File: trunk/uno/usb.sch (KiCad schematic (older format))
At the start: 20 parts, among them U3 ATMEGA16U2-MU(R), X2 USB-MINI-AB

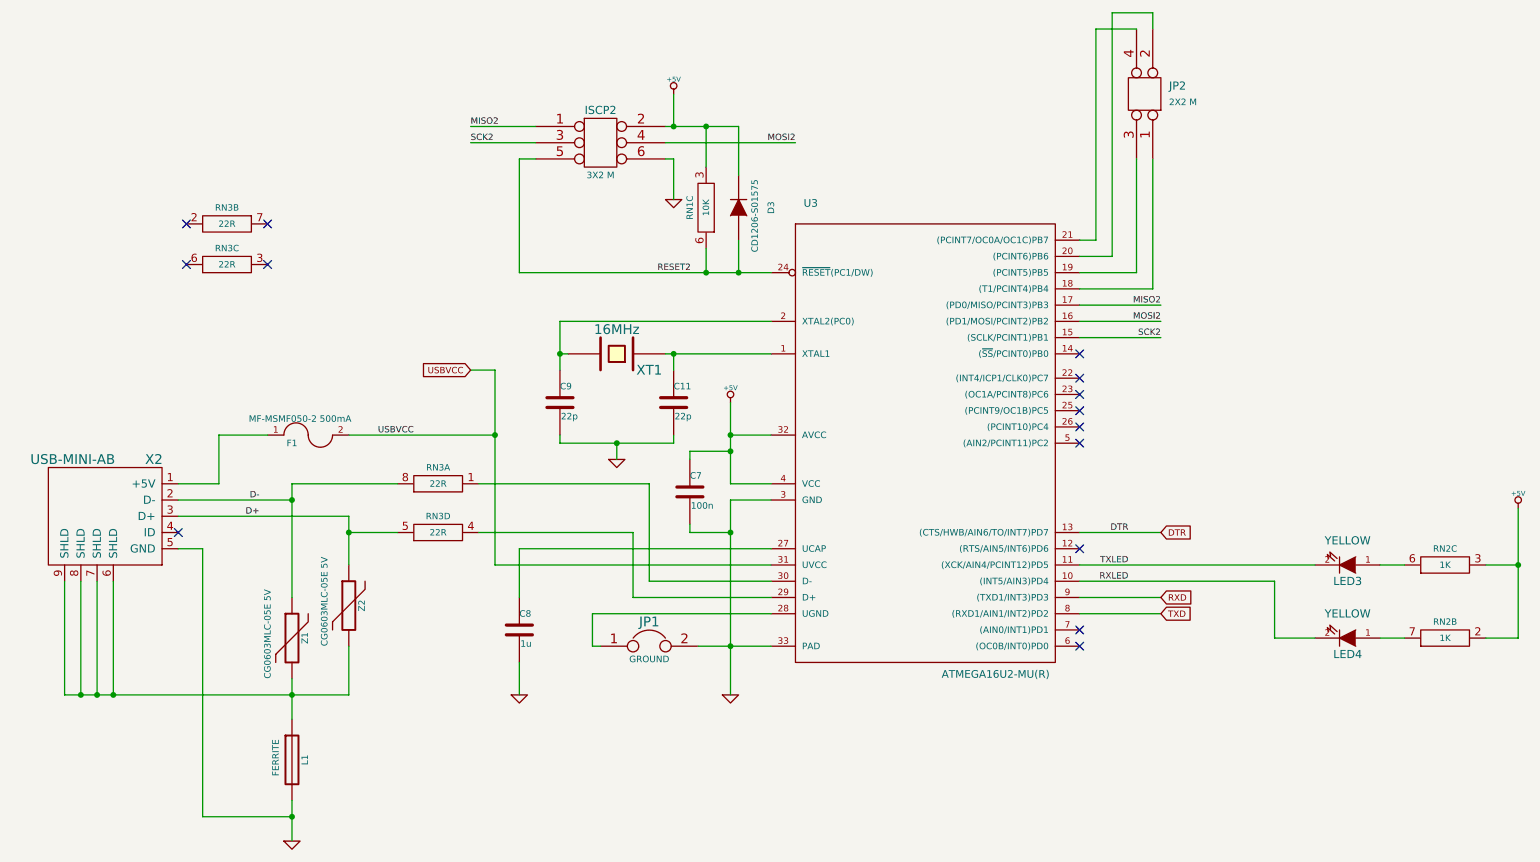
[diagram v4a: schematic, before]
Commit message: All components placed. Some routing started.
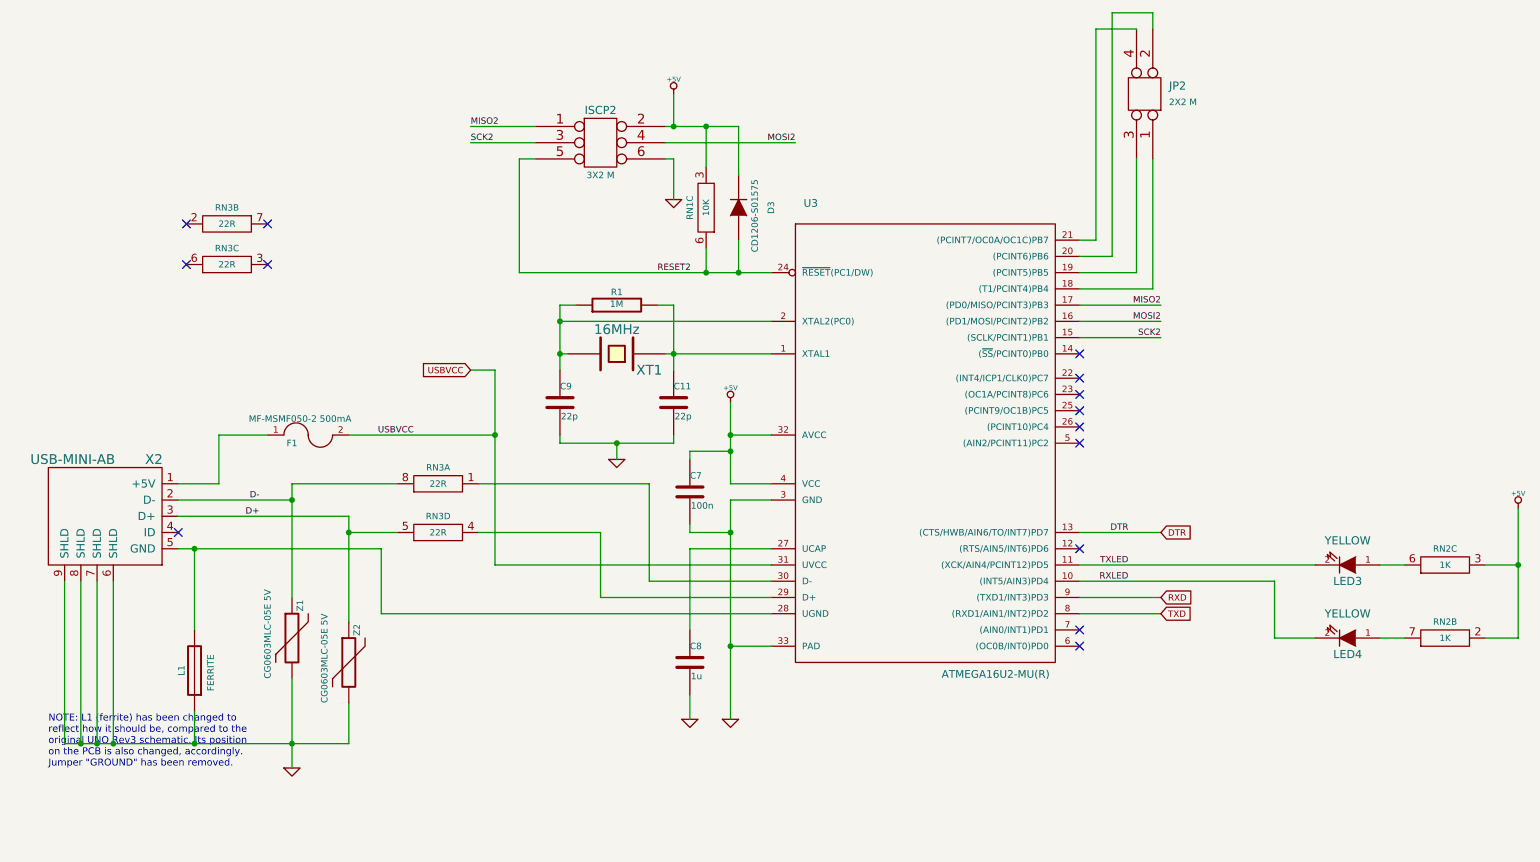
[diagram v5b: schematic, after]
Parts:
- removed JP1: GROUND, JSOLD, symbol JUMPER
- added R1: 1M, ~, symbol R
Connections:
- net GND: now also L1.1, X2.6 (SHLD), X2.7 (SHLD), X2.8 (SHLD), X2.9 (SHLD), Z1.2, Z2.2; no longer L1.2, X2.5 (GND)
- net at C11.1, U3.1 (XTAL1), XT1.1: now also R1.2
- net at C9.1, U3.2 (XTAL2(PC0)), XT1.2: now also R1.1
- net at U3.28 (UGND): now also L1.2, X2.5 (GND)
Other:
- note added: "NOTE: L1 (ferrite) has been changed to\nreflect how it should be, compared to the\noriginal UNO Rev3 schematic. Its position\non the PCB is also changed, accordingly.\nJumper "GROUND" has been removed."
- moved on the sheet: C8, L1, Z2
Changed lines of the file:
@@
 Sheet 2 3
 Title "KiCADuino UNO Rev3"
-Date "25 jul 2013"
+Date "26 jul 2013"
 Rev "0.1"
 Comp "Gruvin & Co"
@@
 L GND #PWR014
 U 1 1 51EFEC35
-P 5450 5500
-F 0 "#PWR014" H 5450 5500 30  0001 C CNN
-F 1 "GND" H 5450 5430 30  0001 C CNN
-F 2 "" H 5450 5500 60  0000 C CNN
-F 3 "" H 5450 5500 60  0000 C CNN
-	1    5450 5500
-	1    0    0    -1
-$EndComp
-$Comp
-L JUMPER JP1
-U 1 1 51EFED7A
-P 4950 5200
-F 0 "JP1" H 4950 5350 60  0000 C CNN
-F 1 "GROUND" H 4950 5120 40  0000 C CNN
-F 2 "JSOLD" H 4950 5200 60  0001 C CNN
-F 3 "~" H 4950 5200 60  0000 C CNN
-	1    4950 5200
+P 5450 5650
+F 0 "#PWR014" H 5450 5650 30  0001 C CNN
+F 1 "GND" H 5450 5580 30  0001 C CNN
+F 2 "" H 5450 5650 60  0000 C CNN
+F 3 "" H 5450 5650 60  0000 C CNN
+	1    5450 5650
 	1    0    0    -1
 $EndComp
@@
 U 1 1 51F00052
 P 2750 5150
-F 0 "Z1" V 2830 5150 40  0000 C CNN
+F 0 "Z1" V 2800 5350 40  0000 C CNN
 F 1 "CG0603MLC-05E 5V" V 2600 4900 40  0000 L CNN
 F 2 "" V 2680 5150 30  0001 C CNN
@@
 L VARISTOR Z2
 U 1 1 51F00069
-P 3100 4950
-F 0 "Z2" V 3180 4950 40  0000 C CNN
-F 1 "CG0603MLC-05E 5V" V 2950 4700 40  0000 L CNN
-F 2 "" V 3030 4950 30  0001 C CNN
-F 3 "~" H 3100 4950 30  0000 C CNN
-	1    3100 4950
+P 3100 5300
+F 0 "Z2" V 3150 5500 40  0000 C CNN
+F 1 "CG0603MLC-05E 5V" V 2950 5050 40  0000 L CNN
+F 2 "" V 3030 5300 30  0001 C CNN
+F 3 "~" H 3100 5300 30  0000 C CNN
+	1    3100 5300
 	1    0    0    -1
 $EndComp
@@
 L GND #PWR017
 U 1 1 51F000AD
-P 2750 6400
-F 0 "#PWR017" H 2750 6400 30  0001 C CNN
-F 1 "GND" H 2750 6330 30  0001 C CNN
-F 2 "" H 2750 6400 60  0000 C CNN
-F 3 "" H 2750 6400 60  0000 C CNN
-	1    2750 6400
+P 2750 5950
+F 0 "#PWR017" H 2750 5950 30  0001 C CNN
+F 1 "GND" H 2750 5880 30  0001 C CNN
+F 2 "" H 2750 5950 60  0000 C CNN
+F 3 "" H 2750 5950 60  0000 C CNN
+	1    2750 5950
 	1    0    0    -1
 $EndComp
@@
 L FERRITE L1
 U 1 1 51F0018C
-P 2750 5900
-F 0 "L1" V 2830 5900 40  0000 C CNN
-F 1 "FERRITE" V 2650 5800 40  0000 L CNN
-F 2 "SM0805" V 2680 5900 30  0001 C CNN
-F 3 "~" H 2750 5900 30  0000 C CNN
-	1    2750 5900
-	1    0    0    -1
-$EndComp
-Wire Wire Line
-	5050 3400 5700 3400
+P 2150 5350
+F 0 "L1" V 2230 5350 40  0000 C CNN
+F 1 "FERRITE" V 2050 5250 40  0000 L CNN
+F 2 "SM0805" V 2080 5350 30  0001 C CNN
+F 3 "~" H 2150 5350 30  0000 C CNN
+	1    2150 5350
+	-1   0    0    1
+$EndComp
+Wire Wire Line
+	5050 3400 5100 3400
+Wire Wire Line
+	5100 3400 5700 3400
 Wire Wire Line
 	5700 3200 4400 3200
 Wire Wire Line
-	4400 3200 4400 3500
+	4400 3100 4400 3200
+Wire Wire Line
+	4400 3200 4400 3400
+Wire Wire Line
+	4400 3400 4400 3500
 Wire Wire Line
 	4400 3400 4450 3400
 Wire Wire Line
-	5100 3500 5100 3400
+	5100 3100 5100 3400
+Wire Wire Line
+	5100 3400 5100 3500
 Connection ~ 5100 3400
 Connection ~ 4400 3400
@@
 	4400 3900 4400 3950
 Wire Wire Line
-	4400 3950 5100 3950
+	4400 3950 4750 3950
+Wire Wire Line
+	4750 3950 5100 3950
 Wire Wire Line
 	5100 3950 5100 3900
@@
 	5450 4200 5700 4200
 Wire Wire Line
-	5450 3700 5450 4200
+	5450 3700 5450 3900
+Wire Wire Line
+	5450 3900 5450 4000
+Wire Wire Line
+	5450 4000 5450 4200
 Wire Wire Line
 	5700 3900 5450 3900
@@
 	5700 4300 5450 4300
 Wire Wire Line
-	5450 4300 5450 5500
-Wire Wire Line
-	5250 5200 5700 5200
+	5450 4300 5450 4500
+Wire Wire Line
+	5450 4500 5450 5200
+Wire Wire Line
+	5450 5200 5450 5650
 Connection ~ 5450 5200
 Wire Wire Line
-	5700 5000 4600 5000
-Wire Wire Line
-	4600 5000 4600 5200
-Wire Wire Line
-	4600 5200 4650 5200
-Wire Wire Line
 	7600 3100 8100 3100
 Wire Wire Line
@@
 	5100 1800 5100 2000
 Wire Wire Line
-	5050 2000 5500 2000
+	5050 2000 5100 2000
+Wire Wire Line
+	5100 2000 5300 2000
+Wire Wire Line
+	5300 2000 5500 2000
 Wire Wire Line
 	5050 2100 5850 2100
@@
 	4250 2000 3850 2000
 Wire Wire Line
-	4150 2900 5700 2900
+	4150 2900 5300 2900
+Wire Wire Line
+	5300 2900 5500 2900
+Wire Wire Line
+	5500 2900 5700 2900
 Wire Wire Line
 	4150 2900 4150 2200
@@
 	7600 5000 8100 5000
 Wire Wire Line
-	2750 6150 2750 6400
-Wire Wire Line
-	2750 5400 2750 5650
-Wire Wire Line
-	3100 5500 3100 5200
-Connection ~ 2750 5500
+	2750 5400 2750 5800
+Wire Wire Line
+	2750 5800 2750 5950
+Wire Wire Line
+	3100 5800 3100 5550
+Connection ~ 2750 5800
 Wire Wire Line
 	2050 4300 2750 4300
 Wire Wire Line
-	2750 4200 2750 4900
+	2750 4200 2750 4300
+Wire Wire Line
+	2750 4300 2750 4900
 Wire Wire Line
 	2750 4200 3400 4200
@@
 	2050 4400 3100 4400
 Wire Wire Line
-	3100 4400 3100 4700
+	3100 4400 3100 4500
+Wire Wire Line
+	3100 4500 3100 5050
 Wire Wire Line
 	3100 4500 3400 4500
@@
 Connection ~ 2750 4300
 Wire Wire Line
-	3900 4500 4850 4500
-Wire Wire Line
-	4850 4500 4850 4900
-Wire Wire Line
-	4850 4900 5700 4900
+	3900 4500 4650 4500
+Wire Wire Line
+	4650 4500 4650 4900
+Wire Wire Line
+	4650 4900 5700 4900
 Wire Wire Line
 	3900 4200 4950 4200
@@
 L C C8
 U 1 1 51F0053A
-P 4150 5100
-F 0 "C8" H 4150 5200 40  0000 L CNN
-F 1 "1u" H 4156 5015 40  0000 L CNN
-F 2 "SM0603_Capa" H 4188 4950 30  0001 C CNN
-F 3 "~" H 4150 5100 60  0000 C CNN
-	1    4150 5100
-	1    0    0    -1
-$EndComp
-Wire Wire Line
-	4150 5300 4150 5500
+P 5200 5300
+F 0 "C8" H 5200 5400 40  0000 L CNN
+F 1 "1u" H 5206 5215 40  0000 L CNN
+F 2 "SM0603_Capa" H 5238 5150 30  0001 C CNN
+F 3 "~" H 5200 5300 60  0000 C CNN
+	1    5200 5300
+	1    0    0    -1
+$EndComp
+Wire Wire Line
+	5200 5500 5200 5650
 $Comp
 L GND #PWR018
 U 1 1 51F005F8
-P 4150 5500
-F 0 "#PWR018" H 4150 5500 30  0001 C CNN
-F 1 "GND" H 4150 5430 30  0001 C CNN
-F 2 "" H 4150 5500 60  0000 C CNN
-F 3 "" H 4150 5500 60  0000 C CNN
-	1    4150 5500
+P 5200 5650
+F 0 "#PWR018" H 5200 5650 30  0001 C CNN
+F 1 "GND" H 5200 5580 30  0001 C CNN
+F 2 "" H 5200 5650 60  0000 C CNN
+F 3 "" H 5200 5650 60  0000 C CNN
+	1    5200 5650
 	1    0    0    -1
 $EndComp
@@
 	5200 4000 5450 4000
 Connection ~ 5450 4000
-Connection ~ 2750 6250
 $Comp
 L FUSE F1
@@
 	2300 3900 2600 3900
 Wire Wire Line
-	5700 4600 4150 4600
-Wire Wire Line
-	4150 4600 4150 4900
+	5700 4600 5200 4600
+Wire Wire Line
+	5200 4600 5200 5100
 Wire Wire Line
 	4000 4700 5700 4700
 Wire Wire Line
-	4000 3500 4000 4700
+	4000 3500 4000 3900
+Wire Wire Line
+	4000 3900 4000 4700
 Wire Wire Line
 	4000 3900 3100 3900
@@
 	10300 5150 10100 5150
 Wire Wire Line
-	10300 4350 10300 5150
+	10300 4350 10300 4700
+Wire Wire Line
+	10300 4700 10300 5150
 Wire Wire Line
 	10100 4700 10300 4700
@@
 $EndComp
 Wire Wire Line
-	1350 5500 3100 5500
-Wire Wire Line
-	2750 6250 2200 6250
-Wire Wire Line
-	2200 6250 2200 4600
-Wire Wire Line
-	2200 4600 2050 4600
-Wire Wire Line
-	1650 4800 1650 5500
-Wire Wire Line
-	1550 4800 1550 5500
-Connection ~ 1650 5500
-Wire Wire Line
-	1450 4800 1450 5500
-Connection ~ 1550 5500
-Wire Wire Line
-	1350 4800 1350 5500
-Connection ~ 1450 5500
+	1350 5800 1450 5800
+Wire Wire Line
+	1450 5800 1550 5800
+Wire Wire Line
+	1550 5800 1650 5800
+Wire Wire Line
+	1650 5800 2150 5800
+Wire Wire Line
+	2150 5800 2750 5800
+Wire Wire Line
+	2750 5800 3100 5800
+Wire Wire Line
+	1650 4800 1650 5800
+Wire Wire Line
+	1550 4800 1550 5800
+Connection ~ 1650 5800
+Wire Wire Line
+	1450 4800 1450 5800
+Connection ~ 1550 5800
+Wire Wire Line
+	1350 4800 1350 5800
+Connection ~ 1450 5800
 NoConn ~ 2050 4500
 $Comp
@@
 NoConn ~ 2100 2850
 NoConn ~ 2100 2600
+$Comp
+L R R1
+U 1 1 51F1FFFF
+P 4750 3100
+F 0 "R1" V 4830 3100 40  0000 C CNN
+F 1 "1M" V 4757 3101 40  0000 C CNN
+F 2 "~" V 4680 3100 30  0000 C CNN
+F 3 "~" H 4750 3100 30  0000 C CNN
+	1    4750 3100
+	0    -1   -1   0
+$EndComp
+Wire Wire Line
+	4500 3100 4400 3100
+Connection ~ 4400 3200
+Wire Wire Line
+	5000 3100 5100 3100
+Wire Wire Line
+	2150 5100 2150 4600
+Connection ~ 2150 4600
+Wire Wire Line
+	2150 5600 2150 5800
+Connection ~ 2150 5800
+Wire Wire Line
+	5700 5200 5450 5200
+Text Notes 1250 5950 0    43   ~ 0
+NOTE: L1 (ferrite) has been changed to\nreflect how it should be, compared to the\noriginal UNO Rev3 schematic. Its position\non the PCB is also changed, accordingly.\nJumper "GROUND" has been removed.
+Wire Wire Line
+	5700 5000 3300 5000
+Wire Wire Line
+	3300 4600 3300 5000
+Wire Wire Line
+	2050 4600 2150 4600
+Wire Wire Line
+	2150 4600 3300 4600
 $EndSCHEMATC

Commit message: More routing.
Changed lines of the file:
@@
 $EndComp
 Wire Wire Line
-	5050 3400 5100 3400
-Wire Wire Line
-	5100 3400 5700 3400
+	5050 3400 5700 3400
 Wire Wire Line
 	5700 3200 4400 3200
 Wire Wire Line
-	4400 3100 4400 3200
-Wire Wire Line
-	4400 3200 4400 3400
-Wire Wire Line
-	4400 3400 4400 3500
+	4400 3100 4400 3500
 Wire Wire Line
 	4400 3400 4450 3400
 Wire Wire Line
-	5100 3100 5100 3400
-Wire Wire Line
-	5100 3400 5100 3500
+	5100 3100 5100 3500
 Connection ~ 5100 3400
 Connection ~ 4400 3400
@@
 	4400 3900 4400 3950
 Wire Wire Line
-	4400 3950 4750 3950
-Wire Wire Line
-	4750 3950 5100 3950
+	4400 3950 5100 3950
 Wire Wire Line
 	5100 3950 5100 3900
@@
 	5450 4200 5700 4200
 Wire Wire Line
-	5450 3700 5450 3900
-Wire Wire Line
-	5450 3900 5450 4000
-Wire Wire Line
-	5450 4000 5450 4200
+	5450 3700 5450 4200
 Wire Wire Line
 	5700 3900 5450 3900
@@
 	5700 4300 5450 4300
 Wire Wire Line
-	5450 4300 5450 4500
-Wire Wire Line
-	5450 4500 5450 5200
-Wire Wire Line
-	5450 5200 5450 5650
+	5450 4300 5450 5650
 Connection ~ 5450 5200
 Wire Wire Line
@@
 	5100 1800 5100 2000
 Wire Wire Line
-	5050 2000 5100 2000
-Wire Wire Line
-	5100 2000 5300 2000
-Wire Wire Line
-	5300 2000 5500 2000
+	5050 2000 5500 2000
 Wire Wire Line
 	5050 2100 5850 2100
@@
 	4250 2000 3850 2000
 Wire Wire Line
-	4150 2900 5300 2900
-Wire Wire Line
-	5300 2900 5500 2900
-Wire Wire Line
-	5500 2900 5700 2900
+	4150 2900 5700 2900
 Wire Wire Line
 	4150 2900 4150 2200
@@
 	7600 5000 8100 5000
 Wire Wire Line
-	2750 5400 2750 5800
-Wire Wire Line
-	2750 5800 2750 5950
+	2750 5400 2750 5950
 Wire Wire Line
 	3100 5800 3100 5550
@@
 	2050 4300 2750 4300
 Wire Wire Line
-	2750 4200 2750 4300
-Wire Wire Line
-	2750 4300 2750 4900
+	2750 4200 2750 4900
 Wire Wire Line
 	2750 4200 3400 4200
@@
 	2050 4400 3100 4400
 Wire Wire Line
-	3100 4400 3100 4500
-Wire Wire Line
-	3100 4500 3100 5050
+	3100 4400 3100 5050
 Wire Wire Line
 	3100 4500 3400 4500
@@
 	4000 4700 5700 4700
 Wire Wire Line
-	4000 3500 4000 3900
-Wire Wire Line
-	4000 3900 4000 4700
+	4000 3500 4000 4700
 Wire Wire Line
 	4000 3900 3100 3900
@@
 	10300 5150 10100 5150
 Wire Wire Line
-	10300 4350 10300 4700
-Wire Wire Line
-	10300 4700 10300 5150
+	10300 4350 10300 5150
 Wire Wire Line
 	10100 4700 10300 4700
@@
 $EndComp
 Wire Wire Line
-	1350 5800 1450 5800
-Wire Wire Line
-	1450 5800 1550 5800
-Wire Wire Line
-	1550 5800 1650 5800
-Wire Wire Line
-	1650 5800 2150 5800
-Wire Wire Line
-	2150 5800 2750 5800
-Wire Wire Line
-	2750 5800 3100 5800
+	1350 5800 3100 5800
 Wire Wire Line
 	1650 4800 1650 5800
@@
 	3300 4600 3300 5000
 Wire Wire Line
-	2050 4600 2150 4600
-Wire Wire Line
-	2150 4600 3300 4600
+	2050 4600 3300 4600
 $EndSCHEMATC

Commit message: Board fully completed v1.0.
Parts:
- added JP1: Solder Bridge, ~, symbol JUMPER
- renumbered X2 to USB1
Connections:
- net GND: now also JP1.1
- net at L1.2, U3.28 (UGND), USB1.5 (GND): now also JP1.2
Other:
- note added: "JP1 exists only as an emergency \nground option for UGND, in case \nL1 becomes fused."
- note added: "NOTE: L1 (ferrite) has been changed to\nreflect how it should be, compared to the\noriginal UNO Rev3 schematic. L1 must be\nrated to minmum 500mA."
- note removed: "NOTE: L1 (ferrite) has been changed to\nreflect how it should be, compared to the\noriginal UNO Rev3 schematic. Its position\non the PCB is also changed, accordingly.\nJumper "GROUND" has been removed."
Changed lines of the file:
@@
 encoding utf-8
 Sheet 2 3
-Title "KiCADuino UNO Rev3"
-Date "26 jul 2013"
-Rev "0.1"
+Title "KiCADuino (based on UNO Rev3)"
+Date "27 jul 2013"
+Rev "v1.0"
 Comp "Gruvin & Co"
 Comment1 ""
@@
 Connection ~ 4000 3900
 $Comp
-L USB-MINI-AB X2
+L USB-MINI-AB USB1
 U 1 1 51F0FF25
 P 1800 4400
-F 0 "X2" H 1900 4750 60  0000 C CNN
+F 0 "USB1" H 1900 4750 60  0000 C CNN
 F 1 "USB-MINI-AB" H 1400 4750 60  0000 C CNN
 F 2 "~" H 1800 4400 60  0000 C CNN
@@
 	5700 5200 5450 5200
 Text Notes 1250 5950 0    43   ~ 0
-NOTE: L1 (ferrite) has been changed to\nreflect how it should be, compared to the\noriginal UNO Rev3 schematic. Its position\non the PCB is also changed, accordingly.\nJumper "GROUND" has been removed.
+NOTE: L1 (ferrite) has been changed to\nreflect how it should be, compared to the\noriginal UNO Rev3 schematic. L1 must be\nrated to minmum 500mA.
 Wire Wire Line
 	5700 5000 3300 5000
 Wire Wire Line
-	3300 4600 3300 5000
-Wire Wire Line
-	2050 4600 3300 4600
+	3300 5000 3300 4600
+Wire Wire Line
+	3300 4600 2050 4600
+$Comp
+L JUMPER JP1
+U 1 1 51F44BD9
+P 3950 5400
+F 0 "JP1" H 3950 5550 60  0000 C CNN
+F 1 "Solder Bridge" H 3950 5320 40  0000 C CNN
+F 2 "~" H 3950 5400 60  0000 C CNN
+F 3 "~" H 3950 5400 60  0000 C CNN
+	1    3950 5400
+	0    -1   -1   0
+$EndComp
+$Comp
+L GND #PWR020
+U 1 1 51F44BE6
+P 3950 5850
+F 0 "#PWR020" H 3950 5850 30  0001 C CNN
+F 1 "GND" H 3950 5780 30  0001 C CNN
+F 2 "" H 3950 5850 60  0000 C CNN
+F 3 "" H 3950 5850 60  0000 C CNN
+	1    3950 5850
+	1    0    0    -1
+$EndComp
+Wire Wire Line
+	3950 5850 3950 5700
+Wire Wire Line
+	3950 5100 3950 5000
+Connection ~ 3950 5000
+Text Notes 3500 6050 0    43   ~ 0
+JP1 exists only as an emergency \nground option for UGND, in case \nL1 becomes fused.
 $EndSCHEMATC
